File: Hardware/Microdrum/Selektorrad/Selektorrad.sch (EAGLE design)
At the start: 11 parts, among them IC1 74AC138N

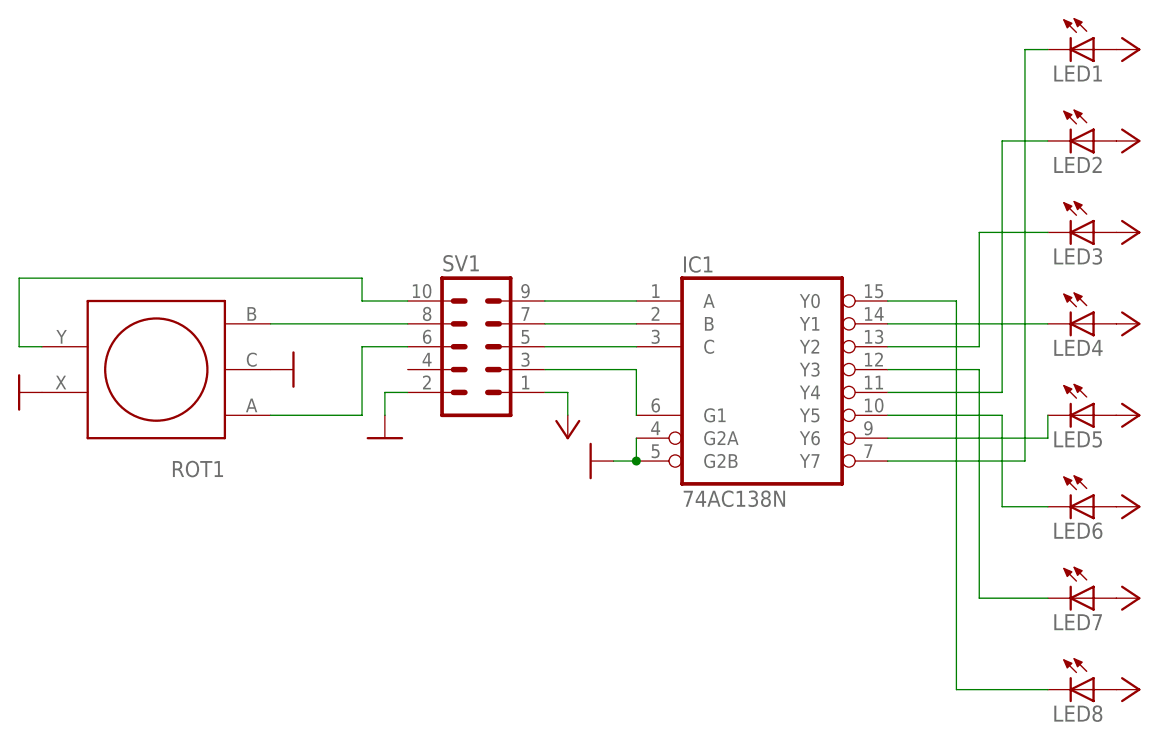
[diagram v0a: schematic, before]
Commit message: minimized selector board
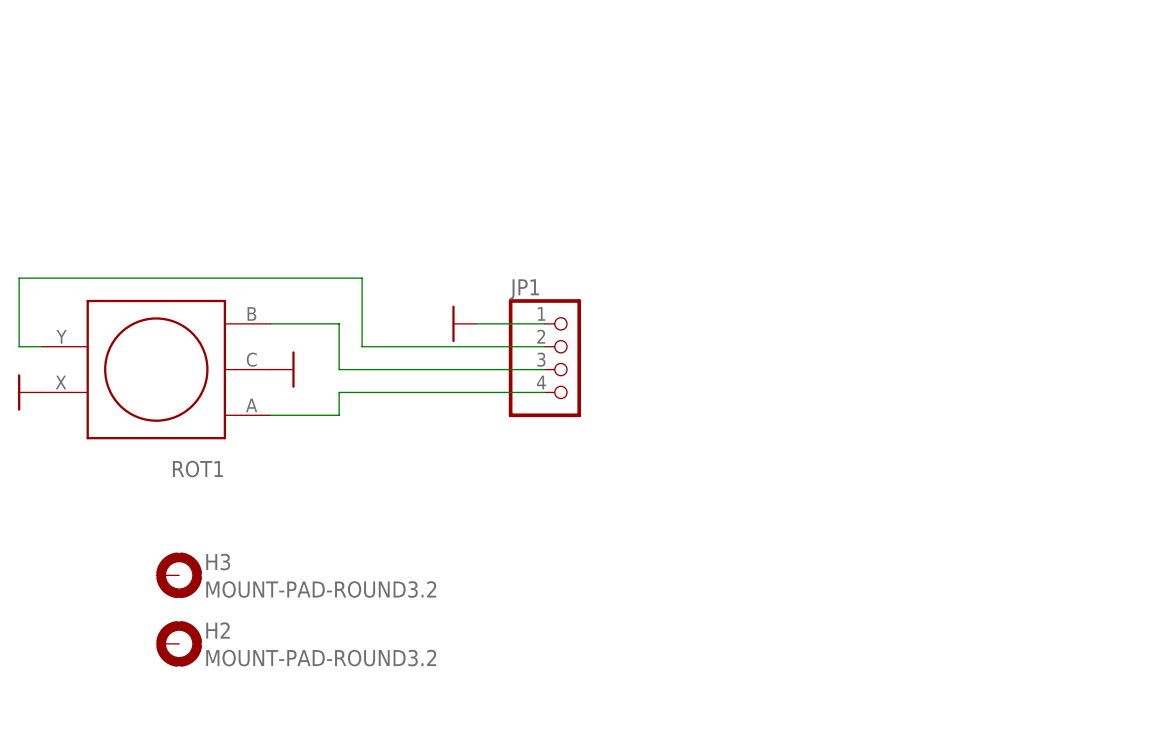
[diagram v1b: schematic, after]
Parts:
- removed IC1: 74AC138N, 74xx-eu:74AC138N
- removed LED1, LED2, LED3, LED4, LED5, LED6, LED7, LED8: (no value), led:LED3MM
- removed SV1: (no value), con-harting-ml:ML10
- added H2, H3: MOUNT-PAD-ROUND3.2, holes:MOUNT-PAD-ROUND3.2
- added JP1: (no value), pinhead:PINHD-1X4
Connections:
- removed net N$10: IC1A.A, SV1.9
- removed net N$11: IC1A.B, SV1.7
- removed net N$12: IC1A.C, SV1.5
- removed net N$13: IC1A.G1, SV1.3
- removed net N$14: ROT1.B, SV1.8
- removed net N$2: IC1A.Y6, LED5.C
- removed net N$3: IC1A.Y5, LED6.C
- removed net N$4: IC1A.Y4, LED2.C
- removed net N$5: IC1A.Y3, LED7.C
- removed net N$7: IC1A.Y2, LED3.C
- removed net N$8: IC1A.Y0, LED8.C
- removed net N$9: IC1A.Y1, LED4.C
- removed net VCC: LED1.A, LED2.A, LED3.A, LED4.A, LED5.A, LED6.A, LED7.A, LED8.A, SV1.1
- net GND: now also JP1.1; no longer IC1A.G2A, IC1A.G2B, SV1.2
- net N$1: now also JP1.3, ROT1.B; no longer IC1A.Y7, LED1.C
- net N$15: now also JP1.2; no longer SV1.10
- net N$6: now also JP1.4; no longer SV1.6
